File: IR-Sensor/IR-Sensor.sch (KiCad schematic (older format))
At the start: 11 parts, among them J1 Conn_01x03_Male, U1 LM324

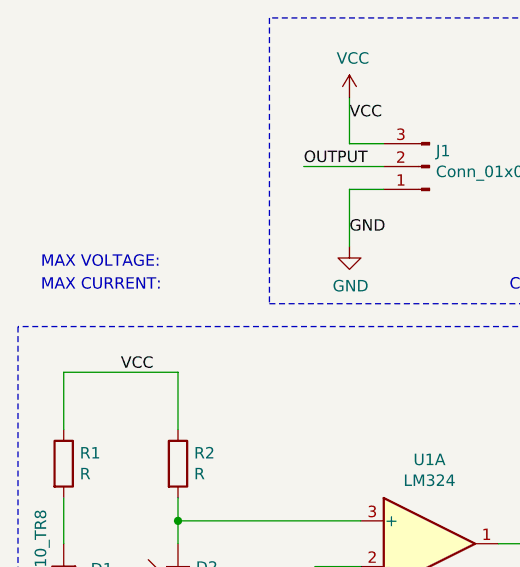
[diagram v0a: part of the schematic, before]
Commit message: Revert "Added reference max current"
This reverts commit 6f043f6b84e07cf2d8713677bb4b91643161c816.
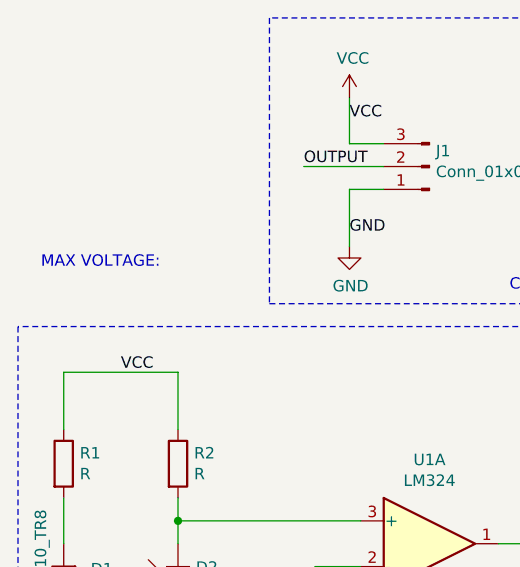
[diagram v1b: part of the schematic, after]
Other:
- note removed: "MAX CURRENT:"
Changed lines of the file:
@@
 Text Notes 4100 3100 0    50   ~ 0
 MAX VOLTAGE:
-Text Notes 4100 3200 0    50   ~ 0
-MAX CURRENT:
 $EndSCHEMATC
